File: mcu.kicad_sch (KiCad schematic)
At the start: 25 parts, among them J1 Conn_01x05, J4 USB_B_Micro, U1 STM32G473CCUx, Y1 8 MHz

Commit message: initial commit, not complete.
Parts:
- removed TP13: GP, TestPoint:TestPoint_Pad_D1.0mm, symbol Connector:TestPoint
- C1, C2, C3, C4, C5, C6, C7, C8, C9: footprint Capacitor_SMD:C_0402_1005Metric -> Capacitor_SMD:C_0603_1608Metric_Pad1.08x0.95mm_HandSolder
- J4: footprint Connector_USB:USB_Micro-B_Molex_47346-0001 -> Connector_USB:USB_Micro-B_Amphenol_10103594-0001LF_Horizontal
- R1, R2, R29, R3, R4, R5: footprint Resistor_SMD:R_0402_1005Metric -> Resistor_SMD:R_0603_1608Metric_Pad0.98x0.95mm_HandSolder
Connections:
- net +3V3: no longer R1.2
- net PTT_IN: now also R29.2, R4.2, U1.2 (PC13); no longer R4.1
- net VDDA: now also R1.2
- new net PTT_IN_5V: R4.1

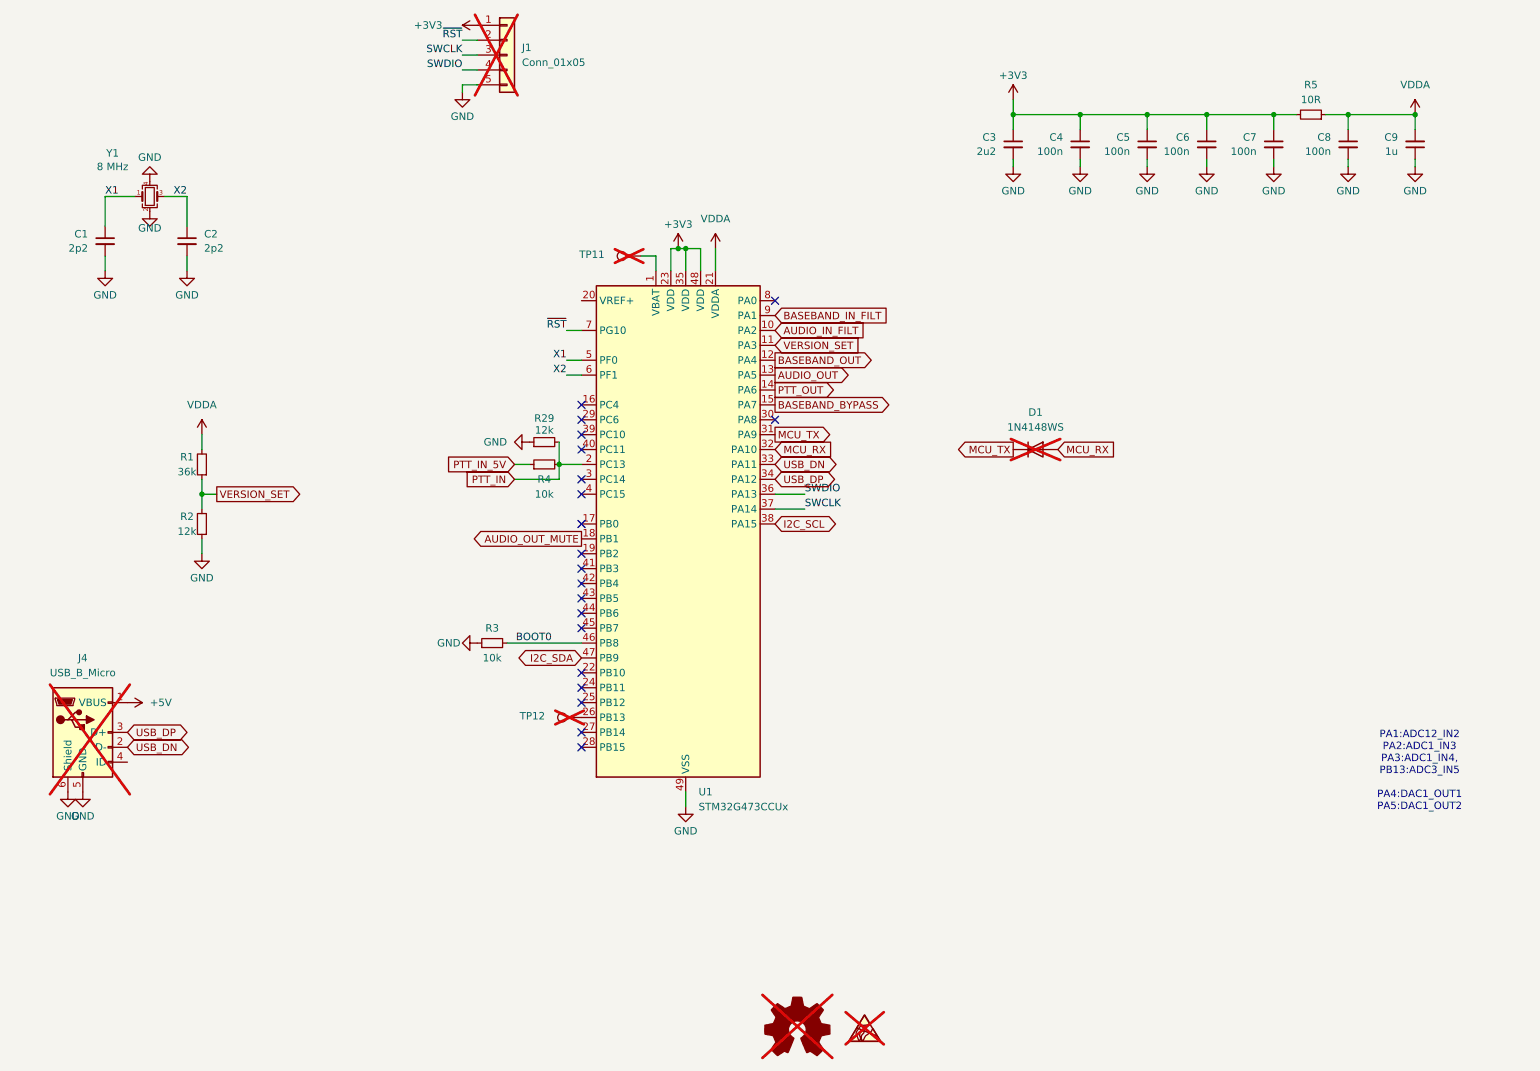
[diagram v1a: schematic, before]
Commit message: PCB shape is created. Most of routing done.
Todo: assign pins for radio control signals.
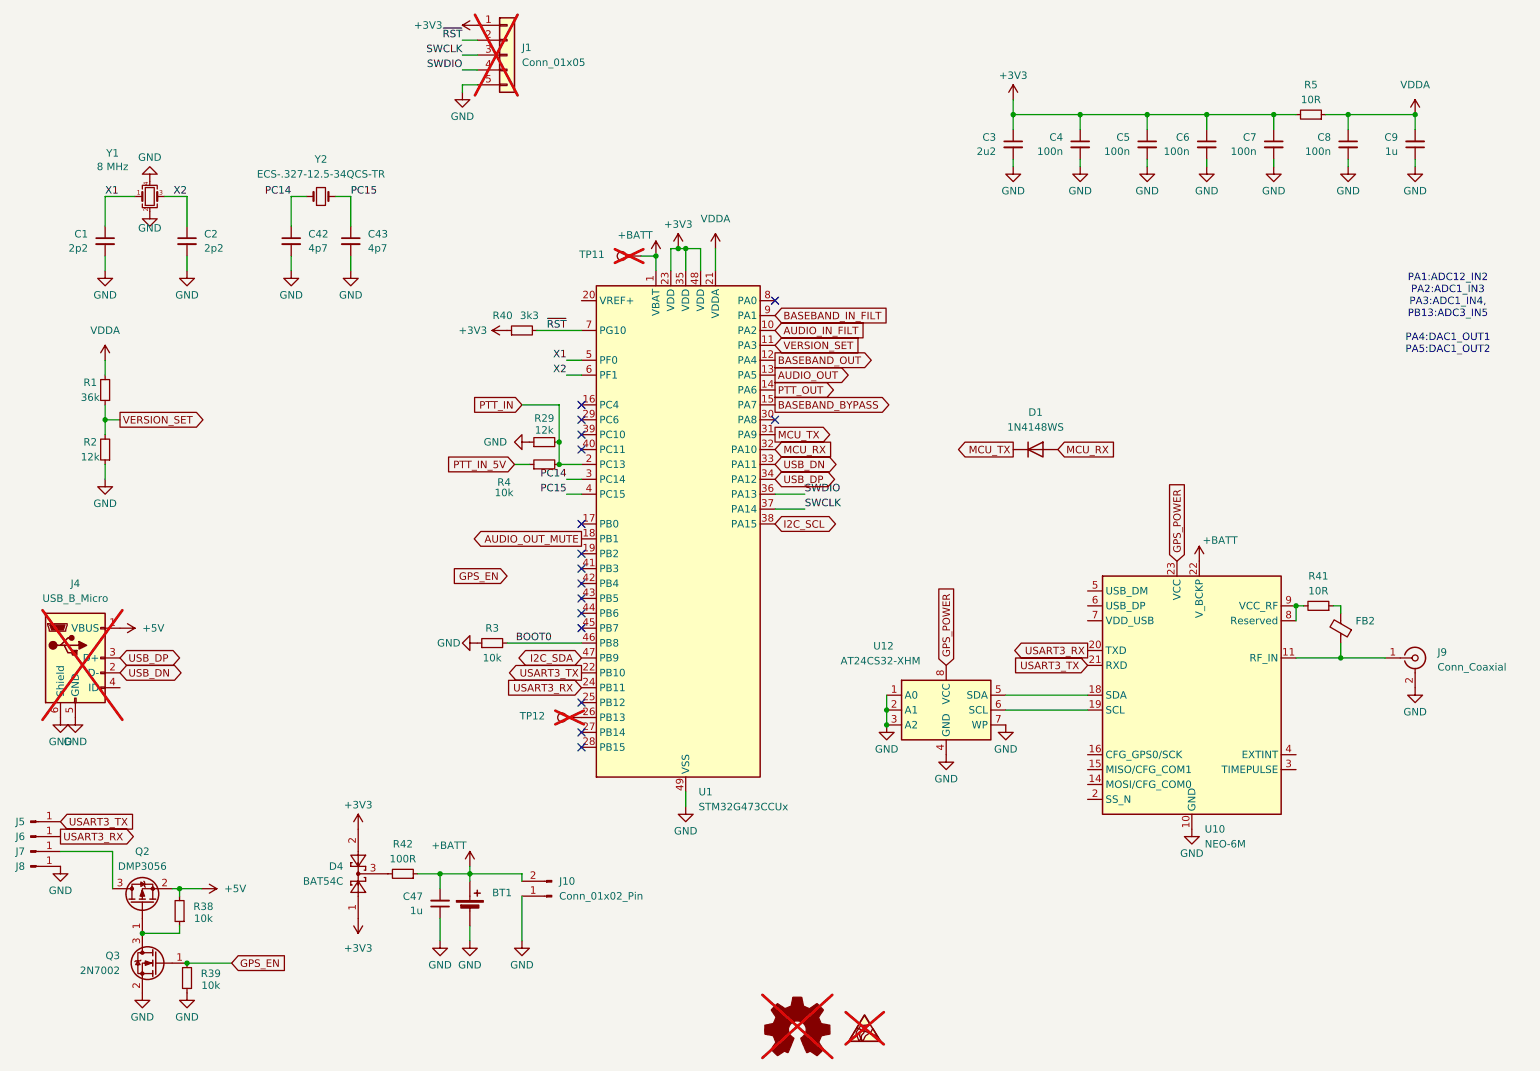
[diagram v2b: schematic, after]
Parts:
- added BT1: Battery_Cell, Battery:BatteryHolder_Keystone_3000_1x12mm, symbol Device:Battery_Cell
- added C42, C43: 4p7, Capacitor_SMD:C_0603_1608Metric_Pad1.08x0.95mm_HandSolder, symbol Device:C_Small
- added C47: 1u, Capacitor_SMD:C_0603_1608Metric_Pad1.08x0.95mm_HandSolder, symbol Device:C_Small
- added D4: BAT54C, Package_TO_SOT_SMD:SOT-23, symbol Diode:BAT54C
- added FB2: FerriteBead_Small, Inductor_SMD:L_0805_2012Metric_Pad1.15x1.40mm_HandSolder, symbol Device:FerriteBead_Small
- added J10: Conn_01x02_Pin, Connector_JST:JST_GH_SM02B-GHS-TB_1x02-1MP_P1.25mm_Horizontal, symbol Connector:Conn_01x02_Pin
- added J5, J6, J7, J8: Conn_01x01_Pin, Connector_Wire:SolderWirePad_1x01_SMD_1x2mm, symbol Connector:Conn_01x01_Pin
- added J9: Conn_Coaxial, Connector_Coaxial:U.FL_Molex_MCRF_73412-0110_Vertical, symbol Connector:Conn_Coaxial
- added Q2: DMP3056, Package_TO_SOT_SMD:SOT-23, symbol Transistor_FET:DMG2301L
- added Q3: 2N7002, Package_TO_SOT_SMD:SOT-23, symbol Transistor_FET:2N7002
- added R38, R39: 10k, Resistor_SMD:R_0603_1608Metric_Pad0.98x0.95mm_HandSolder, symbol Device:R_Small
- added R40: 3k3, Resistor_SMD:R_0603_1608Metric_Pad0.98x0.95mm_HandSolder, symbol Device:R_Small
- added R41: 10R, Resistor_SMD:R_0603_1608Metric_Pad0.98x0.95mm_HandSolder, symbol Device:R_Small
- added R42: 100R, Resistor_SMD:R_0805_2012Metric_Pad1.20x1.40mm_HandSolder, symbol Device:R_Small
- added U10: NEO-6M, RF_GPS:ublox_NEO, symbol micro17:NEO-6M
- added U12: AT24CS32-XHM, Package_SO:TSSOP-8_4.4x3mm_P0.65mm, symbol Memory_EEPROM:AT24CS32-XHM
- added Y2: ECS-.327-12.5-34QCS-TR, Crystal:Crystal_SMD_EuroQuartz_EQ161-2Pin_3.2x1.5mm_HandSoldering, symbol Device:Crystal_Small
- D1: now fitted
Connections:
- net +3V3: now also D4.1, D4.2, R40.1
- net +5V: now also Q2.2 (S), R38.2
- net GND: now also BT1.2 (-), C42.2, C43.2, C47.1, J10.1 (Pin_1), J8.1 (Pin_1), J9.2 (Ext), Q3.2 (S), R39.1, U10.10 (GND), U10.12 (GND), U10.13 (GND), U10.24 (GND), U12.1 (A0), U12.2 (A1), U12.3 (A2), U12.4 (GND), U12.7 (WP)
- net ~{RST}: now also R40.2
- net +BATT: now reaches TP11.1, U1.1 (VBAT)
- net +BATT: now also BT1.1 (+), C47.2, J10.2 (Pin_2), R42.1, U10.22 (V_BCKP)
- net USART3_TX: now reaches U1.22 (PB10)
- net USART3_TX: now also J5.1 (Pin_1), U10.21 (RXD)
- net USART3_RX: now reaches U1.24 (PB11)
- net USART3_RX: now also J6.1 (Pin_1), U10.20 (TXD)
- net PC14: now reaches U1.3 (PC14)
- net PC14: now also C42.1, Y2.1
- net PC15: now reaches U1.4 (PC15)
- net PC15: now also C43.1, Y2.2
- new net: FB2.1, J9.1 (In), U10.11 (RF_IN)
- new net: U10.18 (SDA), U12.5 (SDA)
- new net: U10.19 (SCL), U12.6 (SCL)
- new net: R41.2, U10.8 (Reserved), U10.9 (VCC_RF)
- new net: FB2.2, R41.1
- new net: Q2.1 (G), Q3.3 (D), R38.1
- new net: J7.1 (Pin_1), Q2.3 (D)
- new net: D4.3, R42.2
- new net GPS_EN: Q3.1 (G), R39.2
- new net GPS_POWER: U10.23 (VCC), U12.8 (VCC)
- no-connect marks 20 -> 16
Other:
- moved on the sheet: J4, R1, R2
